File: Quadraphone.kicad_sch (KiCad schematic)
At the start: 38 parts, among them J1 Conn_01x10_Male, J2 Conn_01x10_Male, J3 Conn_01x10_Male, J4 Conn_01x10_Male, J5 Eurorack_10_pin_power, U1 AMS1117-5.0, U14 LM4040DBZ-2.5, U3 MCP6002, U4 LM4040DBZ-5, U5 MCP6004, U8 4066

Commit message: Added readme
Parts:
- U8: value 4066 -> 74LV4066PW
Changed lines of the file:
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@@
       (effects (font (size 1.27 1.27)) (justify left))
     )
-    (property "Value" "4066" (id 1) (at 118.11 171.4499 0)
+    (property "Value" "74LV4066PW" (id 1) (at 118.11 171.4499 0)
       (effects (font (size 1.27 1.27)) (justify left))
     )
@@
       (effects (font (size 1.27 1.27)) hide)
     )
-    (property "Datasheet" "http://www.ti.com/lit/ds/symlink/cd4066b.pdf" (id 3) (at 111.76 170.18 0)
+    (property "Datasheet" "https://www.nexperia.com/products/analog-logic-ics/i-o-expansion-logic/analog-switches/74LV4066PW.html" (id 3) (at 111.76 170.18 0)
       (effects (font (size 1.27 1.27)) hide)
     )
@@
     )
     (path "/07c473a3-19f8-4492-9997-b494b1996c87/9dcec774-4f2b-46a5-88ad-d15c84115c9e"
-      (reference "U6") (unit 1) (value "4066") (footprint "Package_SO:TSSOP-14_4.4x5mm_P0.65mm")
+      (reference "U6") (unit 1) (value "74LV4066PW") (footprint "Package_SO:TSSOP-14_4.4x5mm_P0.65mm")
     )
     (path "/07c473a3-19f8-4492-9997-b494b1996c87/4cd3c34b-83d0-4534-aa14-0d85f7c3aaf2"
-      (reference "U6") (unit 2) (value "4066") (footprint "Package_SO:TSSOP-14_4.4x5mm_P0.65mm")
+      (reference "U6") (unit 2) (value "74LV4066PW") (footprint "Package_SO:TSSOP-14_4.4x5mm_P0.65mm")
     )
     (path "/07c473a3-19f8-4492-9997-b494b1996c87/2ee7557a-4e53-4b59-9973-9e13687ca02f"
-      (reference "U6") (unit 3) (value "4066") (footprint "Package_SO:TSSOP-14_4.4x5mm_P0.65mm")
+      (reference "U6") (unit 3) (value "74LV4066PW") (footprint "Package_SO:TSSOP-14_4.4x5mm_P0.65mm")
     )
     (path "/07c473a3-19f8-4492-9997-b494b1996c87/ad8983ec-8d9a-435a-be19-2f987c16e449"
-      (reference "U6") (unit 4) (value "4066") (footprint "Package_SO:TSSOP-14_4.4x5mm_P0.65mm")
+      (reference "U6") (unit 4) (value "74LV4066PW") (footprint "Package_SO:TSSOP-14_4.4x5mm_P0.65mm")
     )
     (path "/07c473a3-19f8-4492-9997-b494b1996c87/9b3c9edb-77d6-46b2-b6d4-84492b65c96f"
-      (reference "U6") (unit 5) (value "4066") (footprint "Package_SO:TSSOP-14_4.4x5mm_P0.65mm")
+      (reference "U6") (unit 5) (value "74LV4066PW") (footprint "Package_SO:TSSOP-14_4.4x5mm_P0.65mm")
     )
     (path "/61a45bbe-3c79-4a58-ba60-939f33076f4c/9dcec774-4f2b-46a5-88ad-d15c84115c9e"
-      (reference "U7") (unit 1) (value "4066") (footprint "Package_SO:TSSOP-14_4.4x5mm_P0.65mm")
+      (reference "U7") (unit 1) (value "74LV4066PW") (footprint "Package_SO:TSSOP-14_4.4x5mm_P0.65mm")
     )
     (path "/61a45bbe-3c79-4a58-ba60-939f33076f4c/4cd3c34b-83d0-4534-aa14-0d85f7c3aaf2"
-      (reference "U7") (unit 2) (value "4066") (footprint "Package_SO:TSSOP-14_4.4x5mm_P0.65mm")
+      (reference "U7") (unit 2) (value "74LV4066PW") (footprint "Package_SO:TSSOP-14_4.4x5mm_P0.65mm")
     )
     (path "/61a45bbe-3c79-4a58-ba60-939f33076f4c/2ee7557a-4e53-4b59-9973-9e13687ca02f"
-      (reference "U7") (unit 3) (value "4066") (footprint "Package_SO:TSSOP-14_4.4x5mm_P0.65mm")
+      (reference "U7") (unit 3) (value "74LV4066PW") (footprint "Package_SO:TSSOP-14_4.4x5mm_P0.65mm")
     )
     (path "/61a45bbe-3c79-4a58-ba60-939f33076f4c/ad8983ec-8d9a-435a-be19-2f987c16e449"
-      (reference "U7") (unit 4) (value "4066") (footprint "Package_SO:TSSOP-14_4.4x5mm_P0.65mm")
+      (reference "U7") (unit 4) (value "74LV4066PW") (footprint "Package_SO:TSSOP-14_4.4x5mm_P0.65mm")
     )
     (path "/61a45bbe-3c79-4a58-ba60-939f33076f4c/9b3c9edb-77d6-46b2-b6d4-84492b65c96f"
-      (reference "U7") (unit 5) (value "4066") (footprint "Package_SO:TSSOP-14_4.4x5mm_P0.65mm")
+      (reference "U7") (unit 5) (value "74LV4066PW") (footprint "Package_SO:TSSOP-14_4.4x5mm_P0.65mm")
     )
     (path "/3fb79cf5-5f43-45eb-8dbe-e7a5213293f8/beb9a537-39c1-4b2b-af21-62b0d7d2f7d1"
-      (reference "U8") (unit 1) (value "4066") (footprint "Package_SO:TSSOP-14_4.4x5mm_P0.65mm")
+      (reference "U8") (unit 1) (value "74LV4066PW") (footprint "Package_SO:TSSOP-14_4.4x5mm_P0.65mm")
     )
     (path "/61a45bbe-3c79-4a58-ba60-939f33076f4c/beb9a537-39c1-4b2b-af21-62b0d7d2f7d1"
-      (reference "U8") (unit 2) (value "4066") (footprint "Package_SO:TSSOP-14_4.4x5mm_P0.65mm")
+      (reference "U8") (unit 2) (value "74LV4066PW") (footprint "Package_SO:TSSOP-14_4.4x5mm_P0.65mm")
     )
     (path "/07c473a3-19f8-4492-9997-b494b1996c87/beb9a537-39c1-4b2b-af21-62b0d7d2f7d1"
-      (reference "U8") (unit 3) (value "4066") (footprint "Package_SO:TSSOP-14_4.4x5mm_P0.65mm")
+      (reference "U8") (unit 3) (value "74LV4066PW") (footprint "Package_SO:TSSOP-14_4.4x5mm_P0.65mm")
     )
     (path "/5a2c2170-f030-4256-a64a-16cf3de949f5/beb9a537-39c1-4b2b-af21-62b0d7d2f7d1"
-      (reference "U8") (unit 4) (value "4066") (footprint "Package_SO:TSSOP-14_4.4x5mm_P0.65mm")
+      (reference "U8") (unit 4) (value "74LV4066PW") (footprint "Package_SO:TSSOP-14_4.4x5mm_P0.65mm")
     )
     (path "/02d76b2c-cb68-42ef-a692-b79350c54bbb"
-      (reference "U8") (unit 5) (value "4066") (footprint "Package_SO:TSSOP-14_4.4x5mm_P0.65mm")
+      (reference "U8") (unit 5) (value "74LV4066PW") (footprint "Package_SO:TSSOP-14_4.4x5mm_P0.65mm")
     )
     (path "/07c473a3-19f8-4492-9997-b494b1996c87/a880f73f-43d6-4748-bf22-7c6acd58624c"
@@
     )
     (path "/3fb79cf5-5f43-45eb-8dbe-e7a5213293f8/9dcec774-4f2b-46a5-88ad-d15c84115c9e"
-      (reference "U11") (unit 1) (value "4066") (footprint "Package_SO:TSSOP-14_4.4x5mm_P0.65mm")
+      (reference "U11") (unit 1) (value "74LV4066PW") (footprint "Package_SO:TSSOP-14_4.4x5mm_P0.65mm")
     )
     (path "/3fb79cf5-5f43-45eb-8dbe-e7a5213293f8/4cd3c34b-83d0-4534-aa14-0d85f7c3aaf2"
-      (reference "U11") (unit 2) (value "4066") (footprint "Package_SO:TSSOP-14_4.4x5mm_P0.65mm")
+      (reference "U11") (unit 2) (value "74LV4066PW") (footprint "Package_SO:TSSOP-14_4.4x5mm_P0.65mm")
     )
     (path "/3fb79cf5-5f43-45eb-8dbe-e7a5213293f8/2ee7557a-4e53-4b59-9973-9e13687ca02f"
-      (reference "U11") (unit 3) (value "4066") (footprint "Package_SO:TSSOP-14_4.4x5mm_P0.65mm")
+      (reference "U11") (unit 3) (value "74LV4066PW") (footprint "Package_SO:TSSOP-14_4.4x5mm_P0.65mm")
     )
     (path "/3fb79cf5-5f43-45eb-8dbe-e7a5213293f8/ad8983ec-8d9a-435a-be19-2f987c16e449"
-      (reference "U11") (unit 4) (value "4066") (footprint "Package_SO:TSSOP-14_4.4x5mm_P0.65mm")
+      (reference "U11") (unit 4) (value "74LV4066PW") (footprint "Package_SO:TSSOP-14_4.4x5mm_P0.65mm")
     )
     (path "/3fb79cf5-5f43-45eb-8dbe-e7a5213293f8/9b3c9edb-77d6-46b2-b6d4-84492b65c96f"
-      (reference "U11") (unit 5) (value "4066") (footprint "Package_SO:TSSOP-14_4.4x5mm_P0.65mm")
+      (reference "U11") (unit 5) (value "74LV4066PW") (footprint "Package_SO:TSSOP-14_4.4x5mm_P0.65mm")
     )
     (path "/61a45bbe-3c79-4a58-ba60-939f33076f4c/a880f73f-43d6-4748-bf22-7c6acd58624c"
@@
     )
     (path "/5a2c2170-f030-4256-a64a-16cf3de949f5/9dcec774-4f2b-46a5-88ad-d15c84115c9e"
-      (reference "U15") (unit 1) (value "4066") (footprint "Package_SO:TSSOP-14_4.4x5mm_P0.65mm")
+      (reference "U15") (unit 1) (value "74LV4066PW") (footprint "Package_SO:TSSOP-14_4.4x5mm_P0.65mm")
     )
     (path "/5a2c2170-f030-4256-a64a-16cf3de949f5/4cd3c34b-83d0-4534-aa14-0d85f7c3aaf2"
-      (reference "U15") (unit 2) (value "4066") (footprint "Package_SO:TSSOP-14_4.4x5mm_P0.65mm")
+      (reference "U15") (unit 2) (value "74LV4066PW") (footprint "Package_SO:TSSOP-14_4.4x5mm_P0.65mm")
     )
     (path "/5a2c2170-f030-4256-a64a-16cf3de949f5/2ee7557a-4e53-4b59-9973-9e13687ca02f"
-      (reference "U15") (unit 3) (value "4066") (footprint "Package_SO:TSSOP-14_4.4x5mm_P0.65mm")
+      (reference "U15") (unit 3) (value "74LV4066PW") (footprint "Package_SO:TSSOP-14_4.4x5mm_P0.65mm")
     )
     (path "/5a2c2170-f030-4256-a64a-16cf3de949f5/ad8983ec-8d9a-435a-be19-2f987c16e449"
-      (reference "U15") (unit 4) (value "4066") (footprint "Package_SO:TSSOP-14_4.4x5mm_P0.65mm")
+      (reference "U15") (unit 4) (value "74LV4066PW") (footprint "Package_SO:TSSOP-14_4.4x5mm_P0.65mm")
     )
     (path "/5a2c2170-f030-4256-a64a-16cf3de949f5/9b3c9edb-77d6-46b2-b6d4-84492b65c96f"
-      (reference "U15") (unit 5) (value "4066") (footprint "Package_SO:TSSOP-14_4.4x5mm_P0.65mm")
+      (reference "U15") (unit 5) (value "74LV4066PW") (footprint "Package_SO:TSSOP-14_4.4x5mm_P0.65mm")
     )
     (path "/5a2c2170-f030-4256-a64a-16cf3de949f5/a8eb861d-4836-400d-abba-b59dd3828a37"

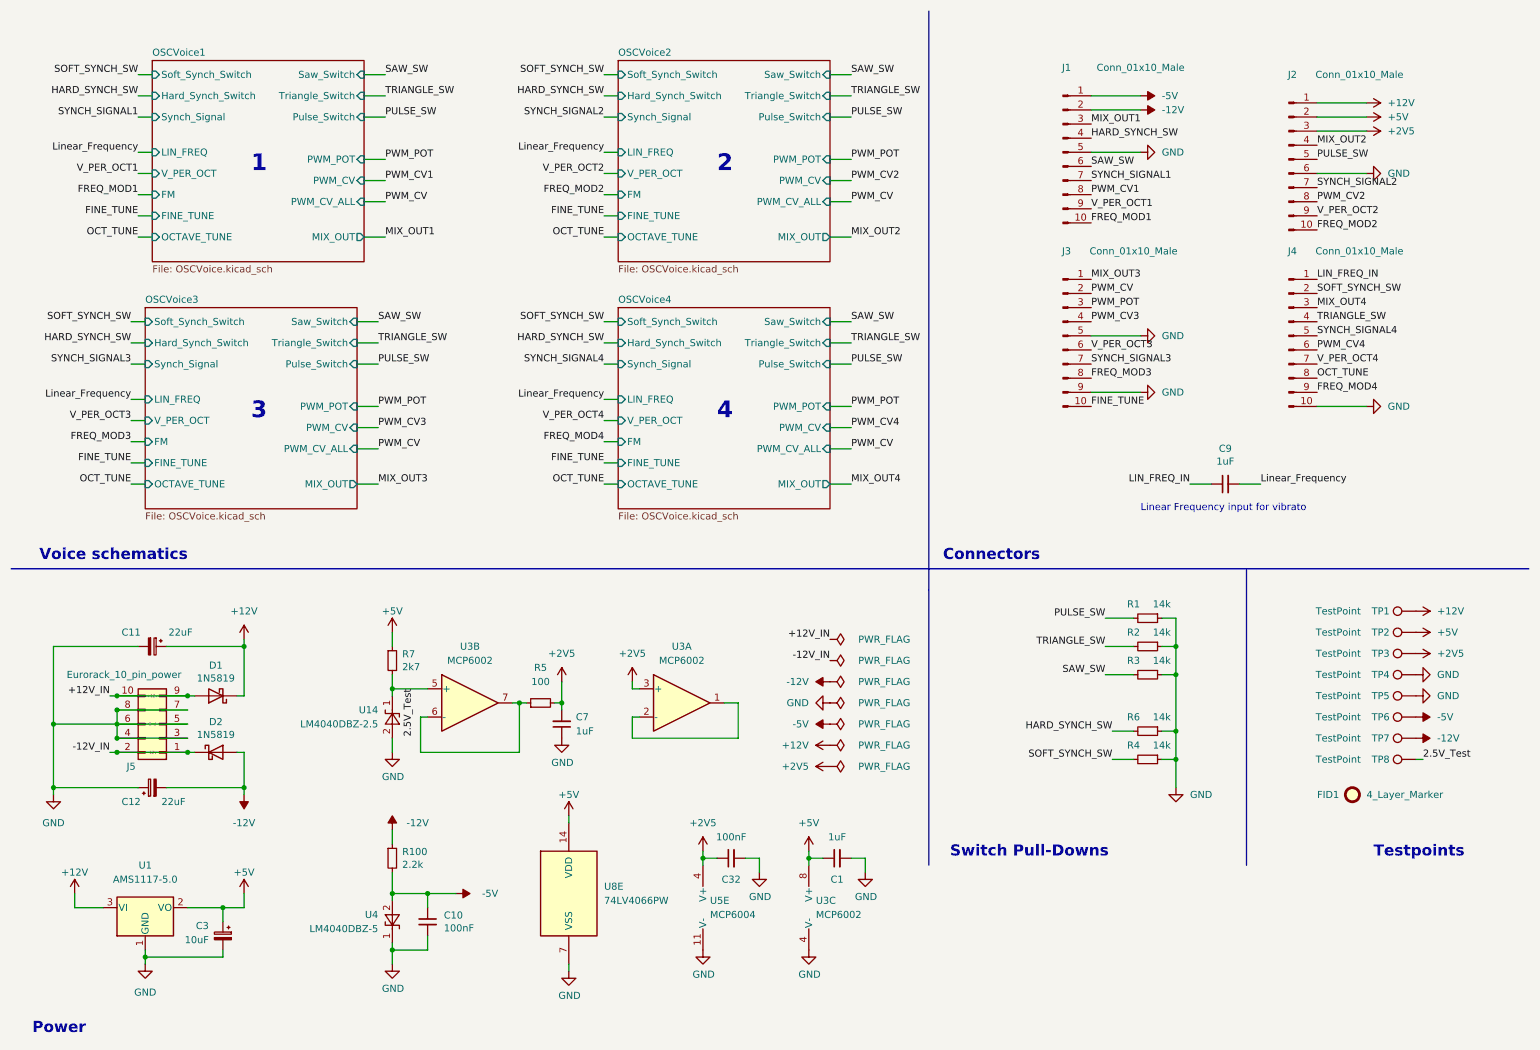
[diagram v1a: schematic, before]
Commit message: v2.0 Update with Synch pulse at start to fix oscillators not starting
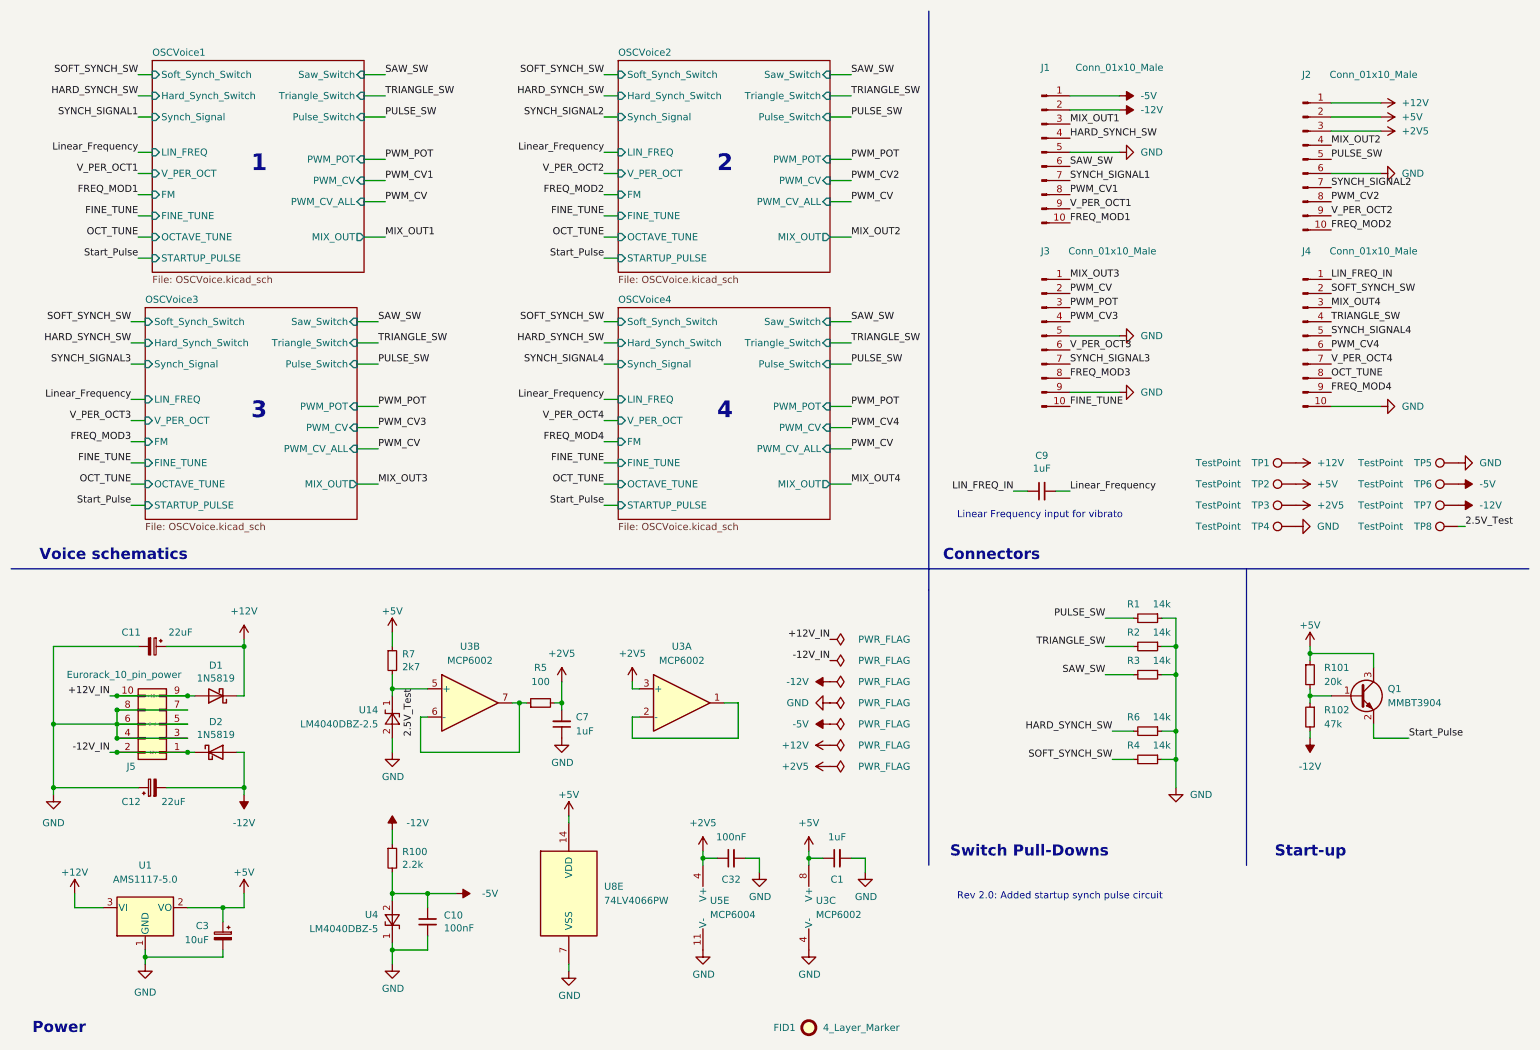
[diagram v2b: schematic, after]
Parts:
- added Q1: MMBT3904, Package_TO_SOT_SMD:SOT-23, symbol Transistor_BJT:MMBT3904
- added R101: 20k, Resistor_SMD:R_0603_1608Metric, symbol Device:R_Small
- added R102: 47k, Resistor_SMD:R_0603_1608Metric, symbol Device:R_Small
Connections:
- net +5V: now also Q1.3 (C), R101.1
- net -12V: now also R102.2
- new net: Q1.1 (B), R101.2, R102.1
- new net Start_Pulse: Q1.2 (E)
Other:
- sheet OSCVoice1 ports: added STARTUP_PULSE; removed none
- sheet OSCVoice2 ports: added STARTUP_PULSE; removed none
- sheet OSCVoice3 ports: added STARTUP_PULSE; removed none
- sheet OSCVoice4 ports: added STARTUP_PULSE; removed none
- note added: "Rev 2.0: Added startup synch pulse circuit"
- note added: "Start-up"
- note removed: "Testpoints"
- moved on the sheet: C9, FID1, J1, J2, J3, J4, TP1, TP2, TP3, TP4, TP5, TP6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

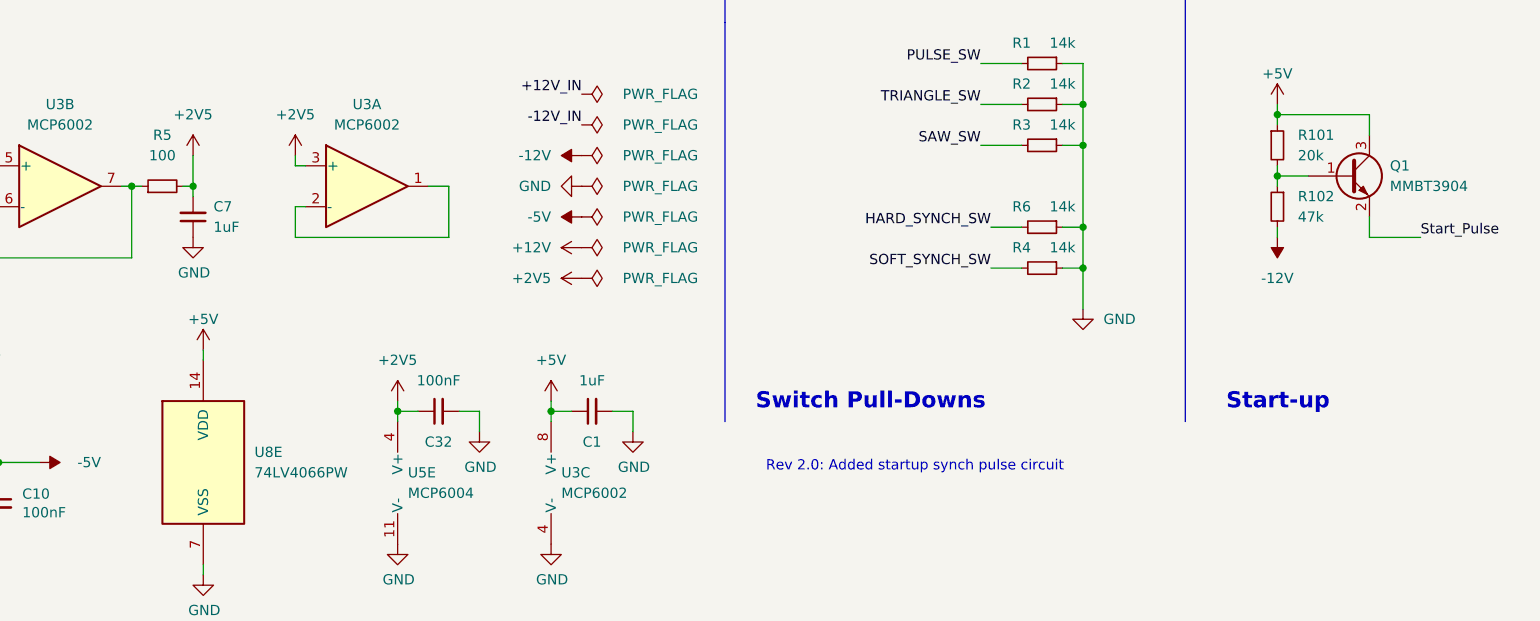
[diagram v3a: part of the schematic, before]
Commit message: Create gerbers for control board changes;
Notes for potential v3 component revision
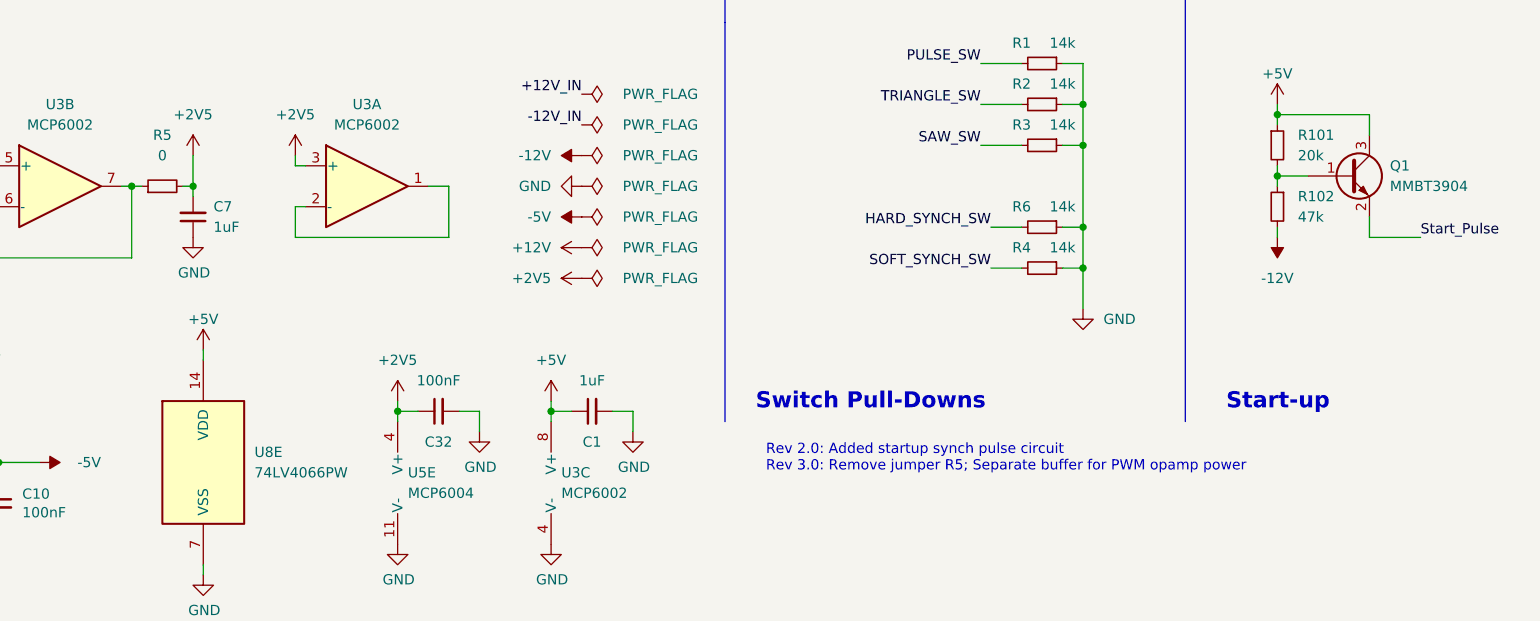
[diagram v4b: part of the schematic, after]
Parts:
- R5: value 100 -> 0
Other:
- note added: "Rev 2.0: Added startup synch pulse circuit Rev 3.0: Remove jumper R5; Separate buffer for PWM opamp power"
- note removed: "Rev 2.0: Added startup synch pulse circuit"
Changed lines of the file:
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@@
     (stroke (width 0) (type default) (color 0 0 0 0))
   )
-  (text "Rev 2.0: Added startup synch pulse circuit" (at 181.61 171.45 0)
+  (text "Rev 2.0: Added startup synch pulse circuit\nRev 3.0: Remove jumper R5; Separate buffer for PWM opamp power\n"
+    (at 181.61 171.45 0)
     (effects (font (size 1.27 1.27)) (justify left bottom))
   )
@@
     (in_bom yes) (on_board yes) (fields_autoplaced)
     (property "Reference" "R5" (id 0) (at 106.68 129.54 90))
-    (property "Value" "100" (id 1) (at 106.68 132.08 90))
+    (property "Value" "0" (id 1) (at 106.68 132.08 90))
     (property "Footprint" "Resistor_SMD:R_0603_1608Metric" (id 2) (at 106.68 135.89 0)
       (effects (font (size 1.27 1.27)) hide)
@@
     )
     (path "/7a15597e-9d4f-4122-b1ab-d8625a3b9e2d"
-      (reference "R5") (unit 1) (value "100") (footprint "Resistor_SMD:R_0603_1608Metric")
+      (reference "R5") (unit 1) (value "0") (footprint "Resistor_SMD:R_0603_1608Metric")
     )
     (path "/bc8395c1-783c-4b85-9f9b-f291e690c543"
